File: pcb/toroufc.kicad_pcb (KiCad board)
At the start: 2 copper layers, 70 x 87 mm, 43 parts, among them J1 HAT, J10 RPAD, J11 POT1-3, J12 POT4-6, J13 REN1, J14 REN2, J15 I2C, J16 Conn_01x04_Male, J2 RKR1-2, J3 RKR3-4, J4 LVR1-2, J5 MASTER-BIG1, J6 BIG2-3-4, J7 NPAD, J8 HPAD, J9 LPAD, U1 BluePill

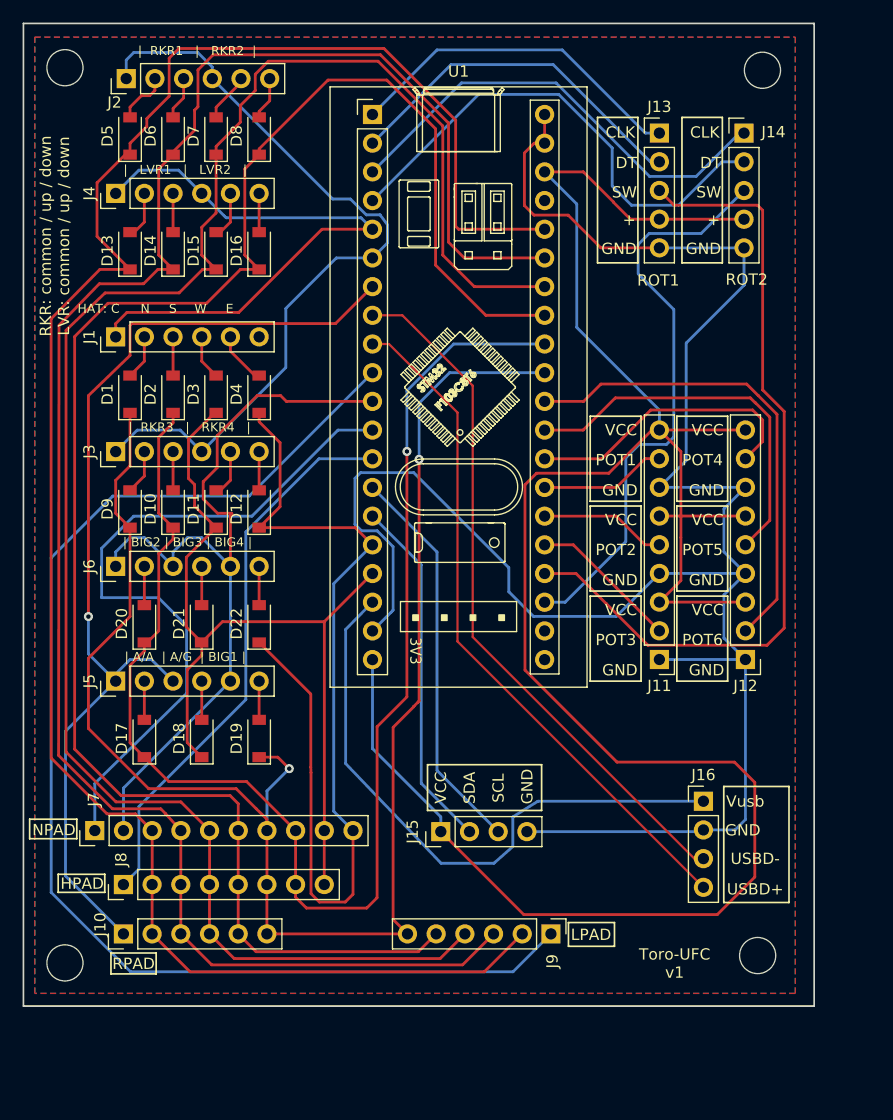
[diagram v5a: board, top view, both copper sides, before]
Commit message: Changing pcb connectors to JST XH
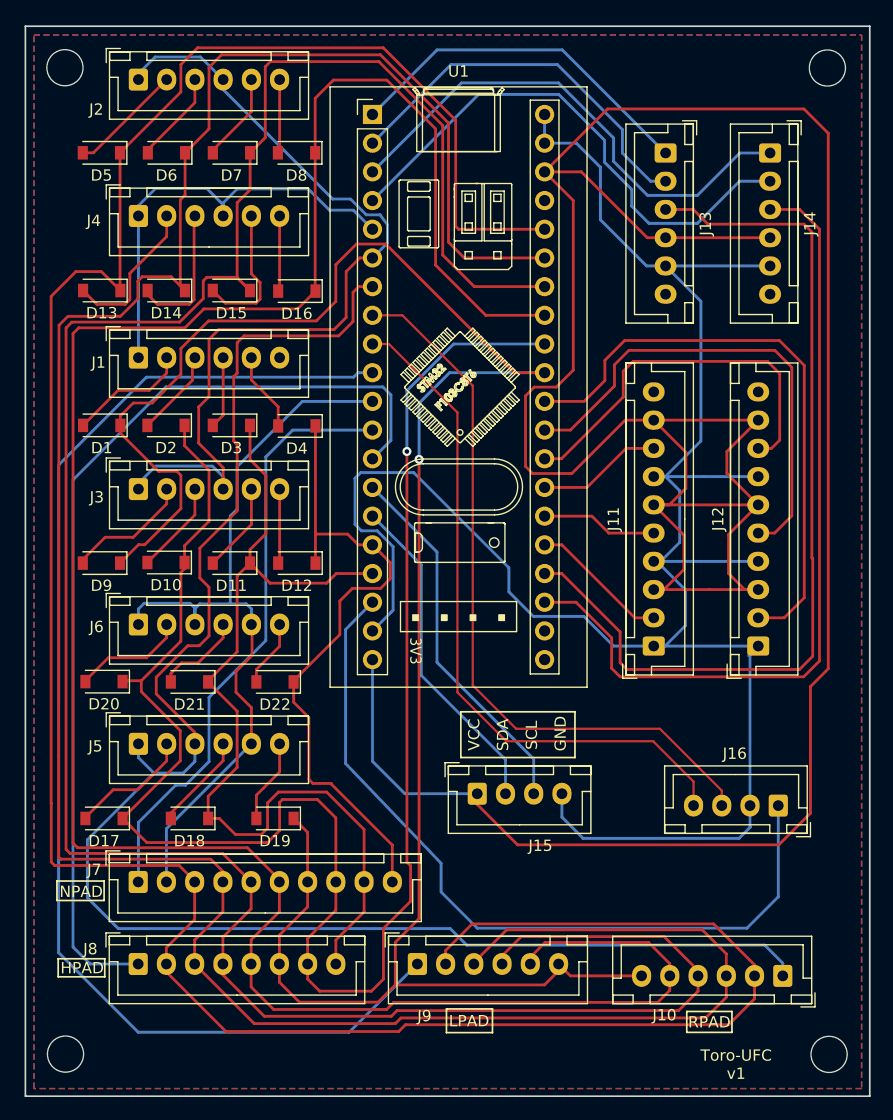
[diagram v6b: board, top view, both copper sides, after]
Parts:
- J1, J10, J2, J3, J4, J5, J6, J9: footprint Connector_PinHeader_2.54mm:PinHeader_1x06_P2.54mm_Vertical -> Connector_JST:JST_XH_B6B-XH-A_1x06_P2.50mm_Vertical
- J11, J12: footprint Connector_PinHeader_2.54mm:PinHeader_1x09_P2.54mm_Vertical -> Connector_JST:JST_XH_B10B-XH-A_1x10_P2.50mm_Vertical
- J13, J14: footprint Connector_PinHeader_2.54mm:PinHeader_1x05_P2.54mm_Vertical -> Connector_JST:JST_XH_B6B-XH-A_1x06_P2.50mm_Vertical
- J15, J16: footprint Connector_PinHeader_2.54mm:PinHeader_1x04_P2.54mm_Vertical -> Connector_JST:JST_XH_B4B-XH-A_1x04_P2.50mm_Vertical
- J7: footprint Connector_PinHeader_2.54mm:PinHeader_1x10_P2.54mm_Vertical -> Connector_JST:JST_XH_B10B-XH-A_1x10_P2.50mm_Vertical
- J8: footprint Connector_PinHeader_2.54mm:PinHeader_1x08_P2.54mm_Vertical -> Connector_JST:JST_XH_B8B-XH-A_1x08_P2.50mm_Vertical
- moved J10 58.5 mm to (176.5, 133.8), turned to 180 degrees
- moved J9 12.1 mm to (144.2, 132.7), turned to 0 degrees
- moved REF** 10.8 mm to (180.6, 140.7)
- moved REF** 8.08 mm to (113.0, 140.7)
- moved D17 7.93 mm to (116.4, 119.8), turned to 180 degrees
- moved D19 7.21 mm to (131.6, 119.8), turned to 180 degrees
- moved D18 7.16 mm to (124.0, 119.8), turned to 180 degrees
- moved J8 7.15 mm to (119.5, 132.7), turned to 0 degrees
- moved J16 6.64 mm to (176.1, 118.7), turned to 180 degrees
- moved D20 6.25 mm to (116.4, 107.7), turned to 180 degrees
- moved J7 5.95 mm to (119.5, 125.5), turned to 0 degrees
- moved J5 5.91 mm to (119.5, 113.2), turned to 0 degrees
- moved D12 5.84 mm to (133.5, 97.2), turned to 180 degrees
- moved REF** 5.75 mm to (180.5, 53.4)
- moved J6 5.53 mm to (119.5, 102.7), turned to 0 degrees
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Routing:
- net VCC: track 199.3 -> 276.5 mm
- net /ROW1: track 172.5 -> 237.0 mm
- net /ROW2: track 167.5 -> 229.1 mm
- net /ROW3: track 162.8 -> 220.1 mm
- net /COL5: track 90.3 -> 144.3 mm, vias 1 -> 0
- net /ROW4: track 157.4 -> 207.2 mm
- net /ROW5: track 142.3 -> 186.2 mm, vias 2 -> 1
- net /COL1: track 49.6 -> 85.9 mm
- net /ROW6: track 123.6 -> 156.9 mm
- net /ROW8: track 83.9 -> 57.7 mm
- net /REN2SW: track 51.5 -> 72.6 mm
- net /Vusb: track 54.3 -> 70.4 mm
- net /COL7: track 53.1 -> 39.5 mm
- net /POT6: track 42.6 -> 52.6 mm
- net /COL2: track 62.8 -> 53.2 mm
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- added copper zone on F.Cu, net GND
- removed copper zone on F.Cu, net VCC
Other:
- board size 70 x 87 mm -> 74.8 x 94.7 mm
- board text removed: "+"
- board text removed: "CLK"
- board text removed: "DT"
- board text removed: "E"
- board text removed: "HAT: C"
- board text removed: "N"
- board text removed: "POT1"
- board text removed: "POT2"
- board text removed: "POT3"
- board text removed: "POT4"
- board text removed: "POT5"
- board text removed: "POT6"
- board text removed: "RKR: common / up / down LVR: common / up / down"
- board text removed: "ROT1"
- board text removed: "ROT2"
- board text removed: "S"
- board text removed: "SW"
- board text removed: "USBD+"
- board text removed: "USBD-"
- board text removed: "Vusb"
- board text removed: "W"
- board text removed: "| A/A | A/G | BIG1 |"
- board text removed: "| BIG2 | BIG3 | BIG4 |"
- board text removed: "| LVR1 | LVR2 |"
- board text removed: "| RKR1 | RKR2 |"
- board text removed: "| RKR3 | RKR4 |"

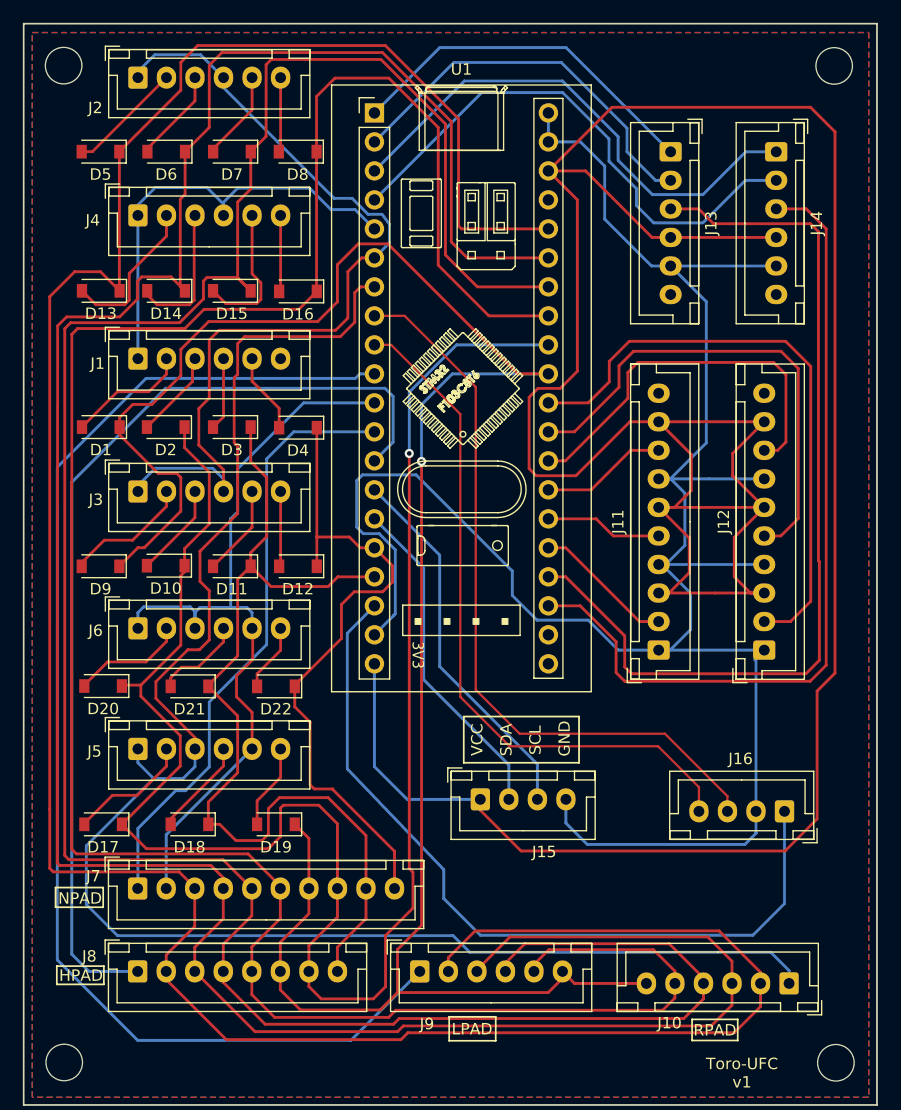
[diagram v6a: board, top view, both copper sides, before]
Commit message: Fixing some lanes.
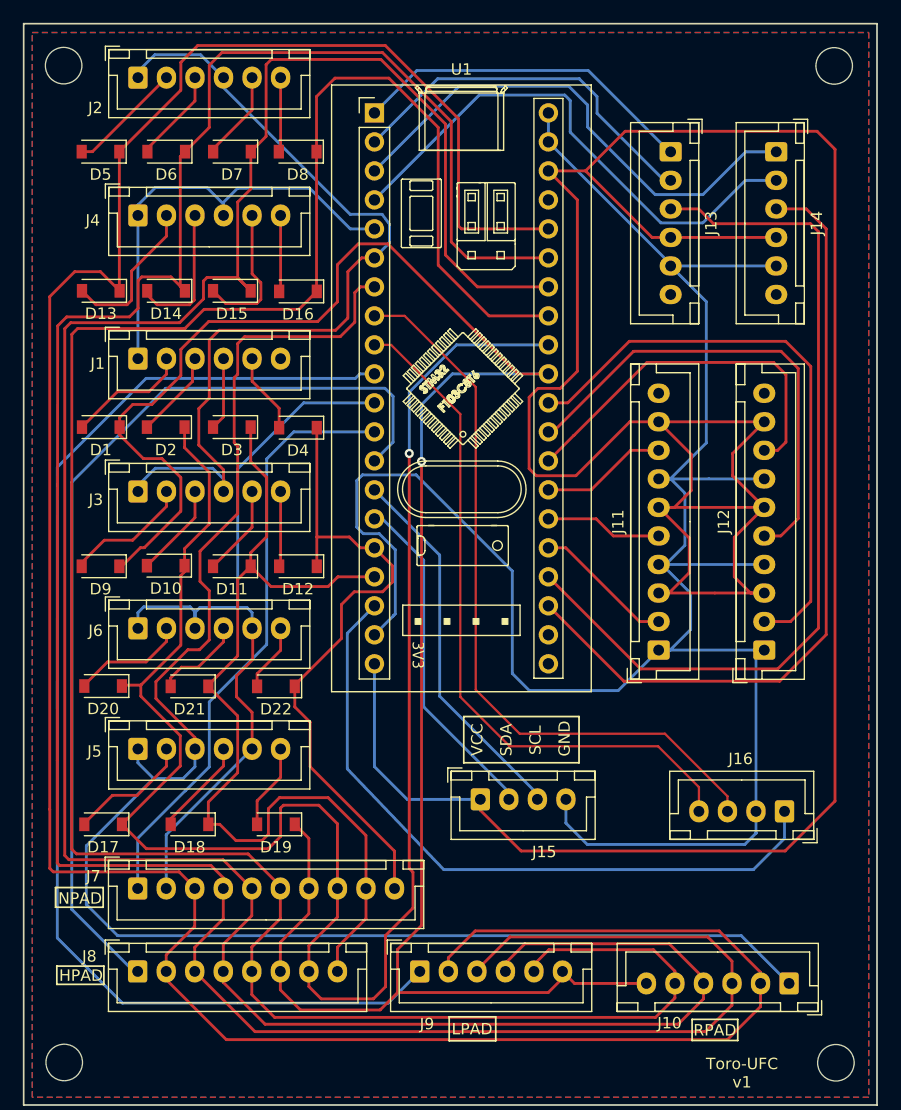
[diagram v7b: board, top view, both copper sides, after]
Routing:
- net /Vusb: track 70.4 -> 60.8 mm
- net VCC: track 276.5 -> 270.6 mm
- net /COL4: track 111.5 -> 107.7 mm
- net /REN1SW: track 80.7 -> 77.0 mm
- net /REN2SW: track 72.6 -> 69.4 mm
- net GND: track 188.9 -> 192.0 mm
- net /COL1: track 85.9 -> 83.6 mm
- net /REN1C: track 32.1 -> 30.4 mm
- net /REN1D: track 34.3 -> 32.8 mm
- net /POT4: track 34.3 -> 32.9 mm
- net /POT5: track 43.3 -> 42.2 mm
- net /POT6: track 52.6 -> 51.5 mm
- net /ROW8: track 57.7 -> 56.7 mm
- net /COL5: track 144.3 -> 143.6 mm
- net /REN2D: track 47.4 -> 46.8 mm
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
